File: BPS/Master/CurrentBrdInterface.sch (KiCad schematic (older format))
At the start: 8 parts, among them J10 CurrentSlaveConnector

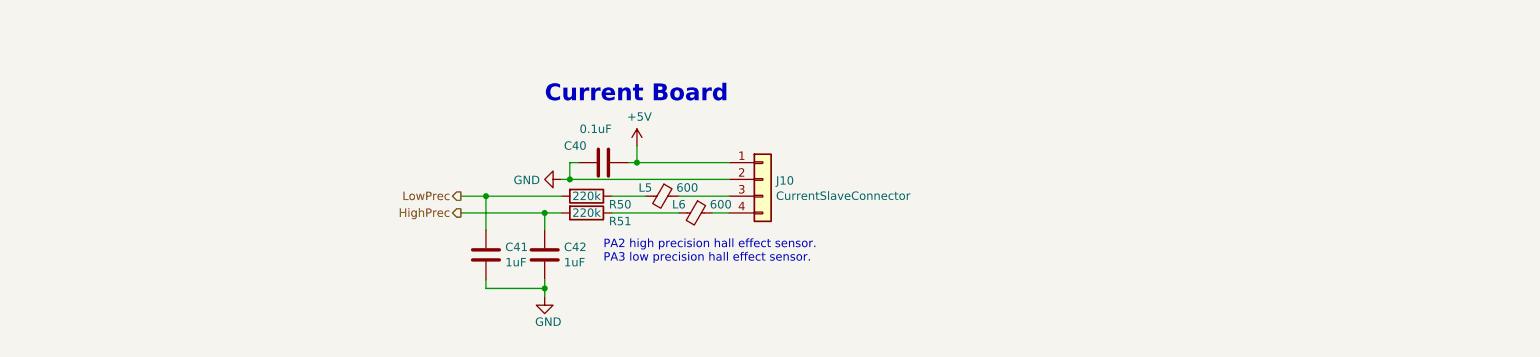
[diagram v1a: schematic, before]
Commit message: Adds BPS master board with no temperature brd electronics and ContactorDriver for dashboard to control.
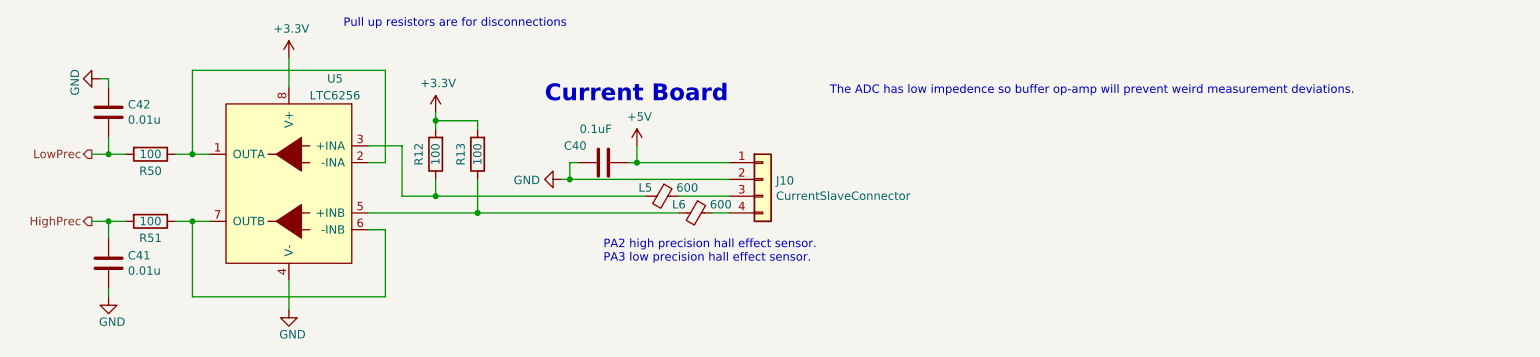
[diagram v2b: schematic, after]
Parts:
- added R12, R13: 100, Resistor_SMD:R_0805_2012Metric, symbol Device:R
- added U5: LTC6256, UTSVT_BPS:LTC6256CTS8-TRMPBF, symbol utsvt-bps:LTC6256
- C41, C42: value 1uF -> 0.01u
- R50, R51: value 220k -> 100
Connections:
- net GND: now also C42.1, U5.4 (V-); no longer C42.2
- net HighPrec: now also C41.1; no longer C42.1
- net LowPrec: now also C42.2; no longer C41.1
- net at R51.1: now also U5.6 (-INB), U5.7 (OUTB); no longer L6.2
- net at R50.1: now also U5.1 (OUTA), U5.2 (-INA); no longer L5.2
- new net: L5.2, R12.1, U5.3 (+INA)
- new net: L6.2, R13.1, U5.5 (+INB)
- new net +3V3: R12.2, R13.2, U5.8 (V+)
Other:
- note added: "Pull up resistors are for disconnections\n"
- note added: "The ADC has low impedence so buffer op-amp will prevent weird measurement deviations."
- moved on the sheet: C41, C42, R50, R51
